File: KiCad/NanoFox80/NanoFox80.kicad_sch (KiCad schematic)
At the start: 53 parts, among them J101 Conn_01x02, J102 Conn_01x02, J111 DB9 Female, J112 Conn_01x02, J113 Conn_01x02, J115 Conn_01x02, P101 ISP/PDI, Q101 BSS84W-7-F, Q102 BSS138W-7-F, SW101 SW_SPST, U101 MC74VHC1G125, U102 LP2985-3.3, U103 SI5351, U104 LP2985-3.3, U105 AVR128DA28, X101 SIT1566AC TCO, X102 25 MHz

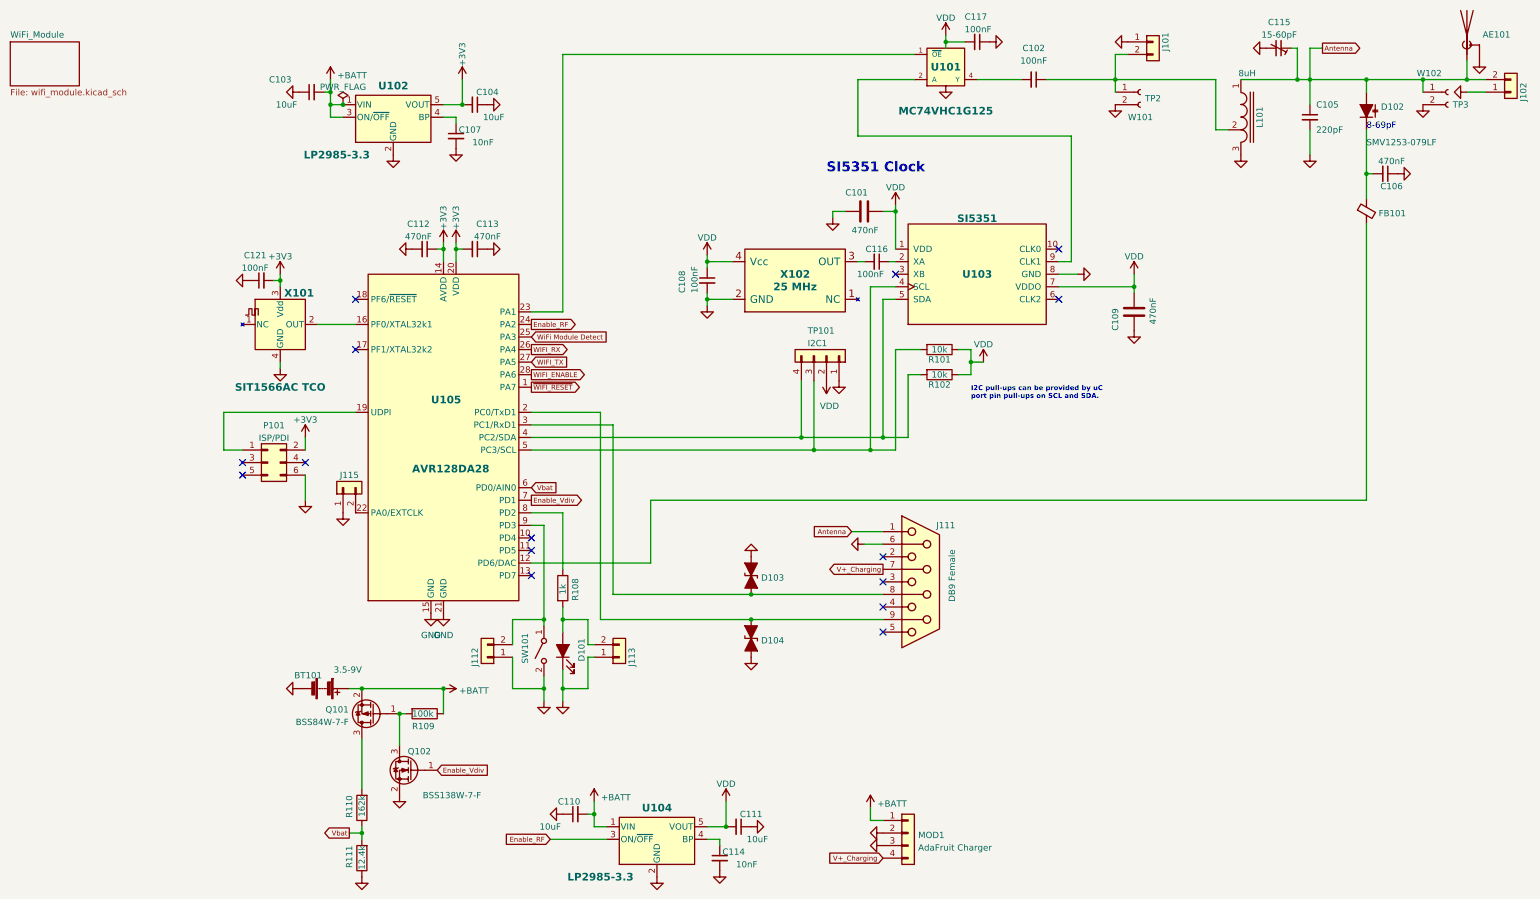
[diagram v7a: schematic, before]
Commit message: Schematic Update
o Updated L101 info
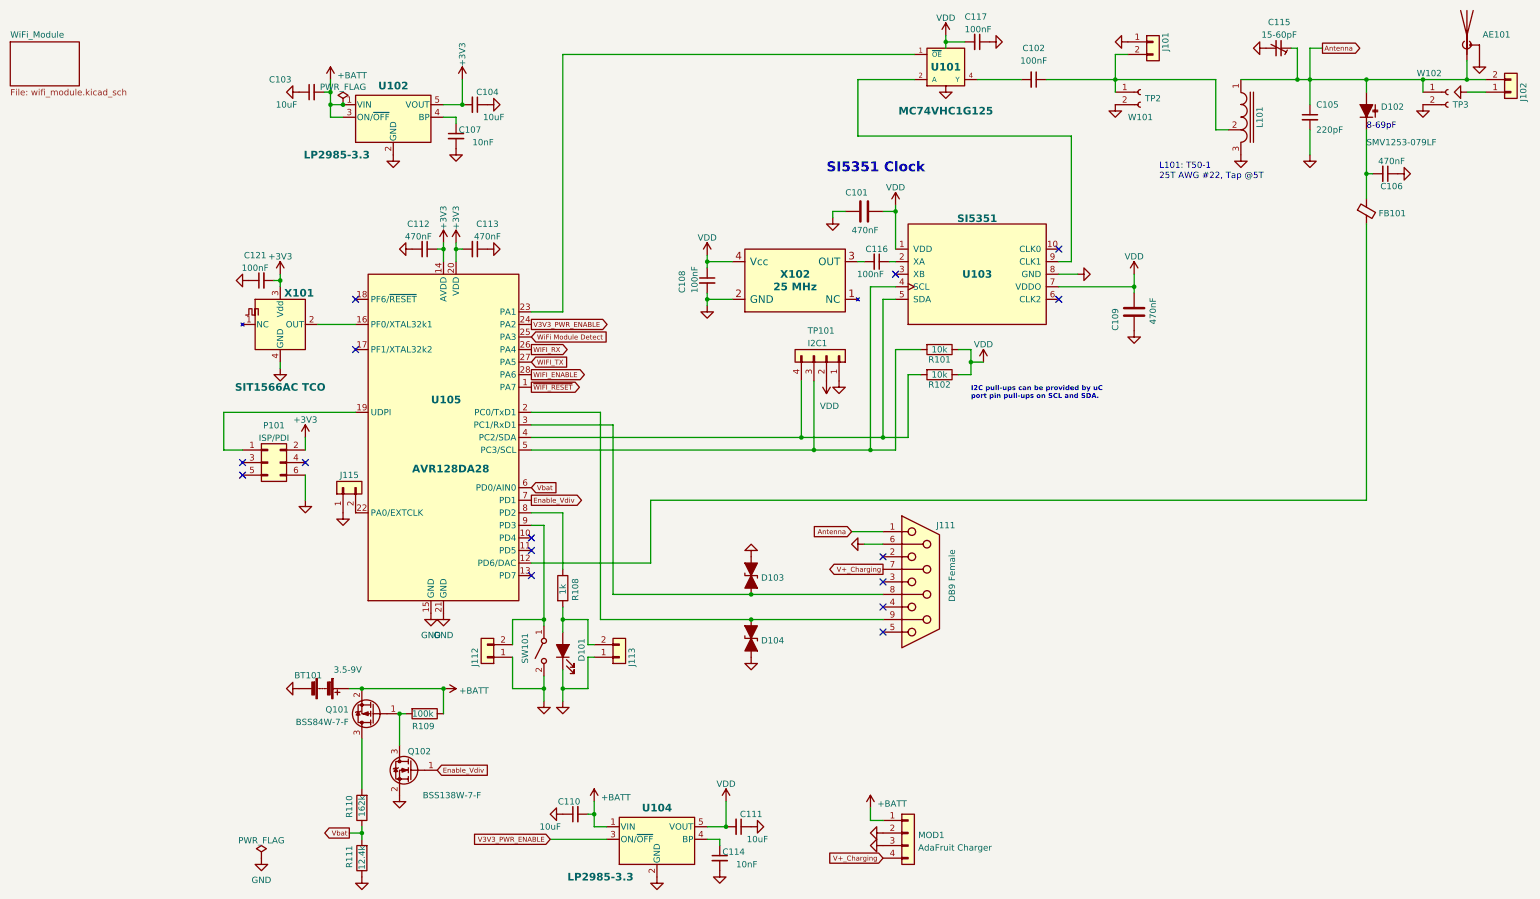
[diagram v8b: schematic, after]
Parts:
- L101: value 8uH -> (none); footprint Transformer_THT:Autotransformer_Toroid_1Tap_Horizontal_D14.0mm_Amidon-T50 -> (none); Digi-Key Part No. FT-50-67 (Amidon) -> T50-1 (Amidon); Link <a href="http://www.amidoncorp.com/ft-50A-43/">Link</a> -> <a href="http://www.amidoncorp.com/T50-1/">Link</a>
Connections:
- net Enable_RF renamed V3V3_PWR_ENABLE
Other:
- note added: "L101: T50-1 25T AWG #22, Tap @5T"
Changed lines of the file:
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@@
+    (effects (font (size 1.27 1.27)) (justify left bottom))
+  )
+  (text "L101: T50-1\n25T AWG #22, Tap @5T " (at 204.47 49.53 0)
     (effects (font (size 1.27 1.27)) (justify left bottom))
   )
@@
     )
   )
-  (global_label "Enable_RF" (shape input) (at 81.28 182.88 180) (fields_autoplaced)
+  (global_label "V3V3_PWR_ENABLE" (shape input) (at 81.28 182.88 180) (fields_autoplaced)
     (effects (font (size 1 1)) (justify right))
-    (property "Intersheet References" "${INTERSHEET_REFS}" (id 0) (at 71.761 182.8175 0)
+    (property "Intersheet References" "${INTERSHEET_REFS}" (id 0) (at 65.5705 182.8175 0)
       (effects (font (size 1 1)) (justify right) hide)
     )
@@
     )
   )
-  (global_label "Enable_RF" (shape output) (at 77.47 78.74 0) (fields_autoplaced)
+  (global_label "V3V3_PWR_ENABLE" (shape output) (at 77.47 78.74 0) (fields_autoplaced)
     (effects (font (size 1 1)) (justify left))
-    (property "Intersheet References" "${INTERSHEET_REFS}" (id 0) (at 86.989 78.6775 0)
+    (property "Intersheet References" "${INTERSHEET_REFS}" (id 0) (at 93.1795 78.6775 0)
       (effects (font (size 1 1)) (justify left) hide)
     )
@@
     )
     (property "Datasheet" "" (id 3) (at 102.87 190.5 0)
+      (effects (font (size 1.27 1.27)) hide)
+    )
+    (pin "1")
+  )
+  (symbol (lib_id "power:PWR_FLAG") (at 22.86 186.69 0) (unit 1)
+    (in_bom yes) (on_board yes) (fields_autoplaced)
+    (property "Reference" "#FLG0102" (id 0) (at 22.86 184.785 0)
+      (effects (font (size 1.27 1.27)) hide)
+    )
+    (property "Value" "PWR_FLAG" (id 1) (at 22.86 183.1142 0))
+    (property "Footprint" "" (id 2) (at 22.86 186.69 0)
+      (effects (font (size 1.27 1.27)) hide)
+    )
+    (property "Datasheet" "~" (id 3) (at 22.86 186.69 0)
       (effects (font (size 1.27 1.27)) hide)
     )
@@
     (pin "1")
   )
+  (symbol (lib_id "power:GND") (at 22.86 186.69 0) (unit 1)
+    (in_bom yes) (on_board yes) (fields_autoplaced)
+    (property "Reference" "#PWR0152" (id 0) (at 22.86 193.04 0)
+      (effects (font (size 1.27 1.27)) hide)
+    )
+    (property "Value" "GND" (id 1) (at 22.86 191.1334 0))
+    (property "Footprint" "" (id 2) (at 22.86 186.69 0)
+      (effects (font (size 1.27 1.27)) hide)
+    )
+    (property "Datasheet" "" (id 3) (at 22.86 186.69 0)
+      (effects (font (size 1.27 1.27)) hide)
+    )
+    (pin "1")
+  )
   (symbol (lib_id "power:GND") (at 30.48 31.75 270) (unit 1)
     (in_bom yes) (on_board yes) (fields_autoplaced)
@@
     (in_bom yes) (on_board yes)
     (property "Reference" "L101" (id 0) (at 224.79 36.83 90))
-    (property "Value" "8uH" (id 1) (at 222.25 27.94 0))
-    (property "Footprint" "Transformer_THT:Autotransformer_Toroid_1Tap_Horizontal_D14.0mm_Amidon-T50" (id 2) (at 222.25 52.07 0)
+    (property "Value" "" (id 1) (at 222.25 27.94 0))
+    (property "Footprint" "" (id 2) (at 222.25 52.07 0)
       (effects (font (size 1.27 1.27)) hide)
     )
@@
       (effects (font (size 1.27 1.27)) hide)
     )
-    (property "Digi-Key Part No." "FT-50-67 (Amidon)" (id 4) (at 220.98 57.15 0)
-      (effects (font (size 1.27 1.27)) hide)
-    )
-    (property "Link" "<a href=\"http://www.amidoncorp.com/ft-50A-43/\">Link</a>" (id 5) (at 224.79 54.61 0)
+    (property "Digi-Key Part No." "T50-1 (Amidon)" (id 4) (at 220.98 57.15 0)
+      (effects (font (size 1.27 1.27)) hide)
+    )
+    (property "Link" "<a href=\"http://www.amidoncorp.com/T50-1/\">Link</a>" (id 5) (at 224.79 54.61 0)
       (effects (font (size 1.524 1.524)) hide)
     )
@@
   (symbol (lib_id "power:VDD") (at 151.13 54.61 0) (unit 1)
     (in_bom yes) (on_board yes) (fields_autoplaced)
-    (property "Reference" "#PWR?" (id 0) (at 151.13 58.42 0)
+    (property "Reference" "#PWR0109" (id 0) (at 151.13 58.42 0)
       (effects (font (size 1.27 1.27)) hide)
     )
@@
   (symbol (lib_id "power:VDD") (at 168.91 86.36 0) (unit 1)
     (in_bom yes) (on_board yes) (fields_autoplaced)
-    (property "Reference" "#PWR?" (id 0) (at 168.91 90.17 0)
+    (property "Reference" "#PWR0112" (id 0) (at 168.91 90.17 0)
       (effects (font (size 1.27 1.27)) hide)
     )
@@
   (symbol (lib_id "power:VDD") (at 199.39 68.58 0) (unit 1)
     (in_bom yes) (on_board yes) (fields_autoplaced)
-    (property "Reference" "#PWR?" (id 0) (at 199.39 72.39 0)
+    (property "Reference" "#PWR0116" (id 0) (at 199.39 72.39 0)
       (effects (font (size 1.27 1.27)) hide)
     )
@@
   (symbol (lib_id "power:VDD") (at 161.29 20.32 0) (unit 1)
     (in_bom yes) (on_board yes) (fields_autoplaced)
-    (property "Reference" "#PWR?" (id 0) (at 161.29 24.13 0)
+    (property "Reference" "#PWR0101" (id 0) (at 161.29 24.13 0)
       (effects (font (size 1.27 1.27)) hide)
     )
@@
   (symbol (lib_id "power:VDD") (at 137.16 90.17 0) (mirror x) (unit 1)
     (in_bom yes) (on_board yes)
-    (property "Reference" "#PWR?" (id 0) (at 137.16 86.36 0)
+    (property "Reference" "#PWR0122" (id 0) (at 137.16 86.36 0)
       (effects (font (size 1.27 1.27)) hide)
     )
@@
   (symbol (lib_id "power:VDD") (at 113.03 64.77 0) (unit 1)
     (in_bom yes) (on_board yes) (fields_autoplaced)
-    (property "Reference" "#PWR?" (id 0) (at 113.03 68.58 0)
+    (property "Reference" "#PWR0121" (id 0) (at 113.03 68.58 0)
       (effects (font (size 1.27 1.27)) hide)
     )
@@
       (reference "#FLG0101") (unit 1) (value "PWR_FLAG") (footprint "")
     )
+    (path "/066be2bb-11b4-4cb6-9380-15c3b0bd6824"
+      (reference "#FLG0102") (unit 1) (value "PWR_FLAG") (footprint "")
+    )
+    (path "/bc11db3d-8aed-45db-b3ba-6913cdd090f7"
+      (reference "#PWR0101") (unit 1) (value "VDD") (footprint "")
+    )
     (path "/69184b35-04b2-4a01-9060-7da95c09e076"
       (reference "#PWR0102") (unit 1) (value "GND") (footprint "")
@@
       (reference "#PWR0108") (unit 1) (value "GND") (footprint "")
     )
+    (path "/4c753411-4935-4d67-a8ce-5961aef2b133"
+      (reference "#PWR0109") (unit 1) (value "VDD") (footprint "")
+    )
     (path "/8e0525c9-ecde-46db-88fa-f01e85921a0e"
       (reference "#PWR0110") (unit 1) (value "GND") (footprint "")
@@
       (reference "#PWR0111") (unit 1) (value "GND") (footprint "")
     )
+    (path "/77e27f46-3057-4ccf-853e-f3e714248f48"
+      (reference "#PWR0112") (unit 1) (value "VDD") (footprint "")
+    )
     (path "/aff8d39f-a36f-4449-822b-3a4ab0ea9c0a"
       (reference "#PWR0113") (unit 1) (value "GND") (footprint "")
@@
       (reference "#PWR0115") (unit 1) (value "GND") (footprint "")
     )
+    (path "/a2a159c9-63ad-4539-ba5a-cb15a88a21fa"
+      (reference "#PWR0116") (unit 1) (value "VDD") (footprint "")
+    )
     (path "/186766a2-f6dc-49c8-bb5e-bedee170e2cc"
       (reference "#PWR0117") (unit 1) (value "GND") (footprint "")
@@
       (reference "#PWR0120") (unit 1) (value "GND") (footprint "")
     )
+    (path "/fa05f24a-ab89-422a-9ec2-854e6797ecca"
+      (reference "#PWR0121") (unit 1) (value "VDD") (footprint "")
+    )
+    (path "/cafb01d1-6637-4402-bb54-06f23929abc7"
+      (reference "#PWR0122") (unit 1) (value "VDD") (footprint "")
+    )
     (path "/7a34d33d-a037-4524-9691-185b2fbdb917"
       (reference "#PWR0123") (unit 1) (value "GND") (footprint "")
@@
       (reference "#PWR0151") (unit 1) (value "GND") (footprint "")
     )
+    (path "/34f0a189-60a5-4ee3-84c4-03829f6e40a8"
+      (reference "#PWR0152") (unit 1) (value "GND") (footprint "")
+    )
     (path "/32134e8d-6f2e-439a-9fd2-4f7c8132a084"
       (reference "#PWR0153") (unit 1) (value "GND") (footprint "")
@@
       (reference "#PWR0209") (unit 1) (value "GND") (footprint "")
     )
-    (path "/4c753411-4935-4d67-a8ce-5961aef2b133"
-      (reference "#PWR?") (unit 1) (value "VDD") (footprint "")
-    )
-    (path "/77e27f46-3057-4ccf-853e-f3e714248f48"
-      (reference "#PWR?") (unit 1) (value "VDD") (footprint "")
-    )
-    (path "/a2a159c9-63ad-4539-ba5a-cb15a88a21fa"
-      (reference "#PWR?") (unit 1) (value "VDD") (footprint "")
-    )
-    (path "/bc11db3d-8aed-45db-b3ba-6913cdd090f7"
-      (reference "#PWR?") (unit 1) (value "VDD") (footprint "")
-    )
-    (path "/cafb01d1-6637-4402-bb54-06f23929abc7"
-      (reference "#PWR?") (unit 1) (value "VDD") (footprint "")
-    )
-    (path "/fa05f24a-ab89-422a-9ec2-854e6797ecca"
-      (reference "#PWR?") (unit 1) (value "VDD") (footprint "")
-    )
     (path "/c938e709-b8e6-465b-a1ac-8390c5f3f4c9"
